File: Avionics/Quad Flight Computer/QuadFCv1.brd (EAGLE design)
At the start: 49.5 x 49.5 mm, 122 parts, among them J2 1050270001, Q1 DMP2035U, Q2 DMP2035U, Q3 DMP2035U, SW1 PTS635VL31-VERT, U1 TM4C123GH6PZ, U10 LTC4412, U11 AP7215-33YG-13, U2 74LVC4245APW, U3 ATMEGA32U2-MU, U5 INVESENSE_MPU-6000, U6 HMC5883LSMD, U7 MS5611-01BA, U8 74AUP1G19GW, U9 S25FL127S, X1 HWB, Y1 32.768KHZ, Y2 AWSCR-20.00CW-T, Y3 PRQC16.00SR5010X000

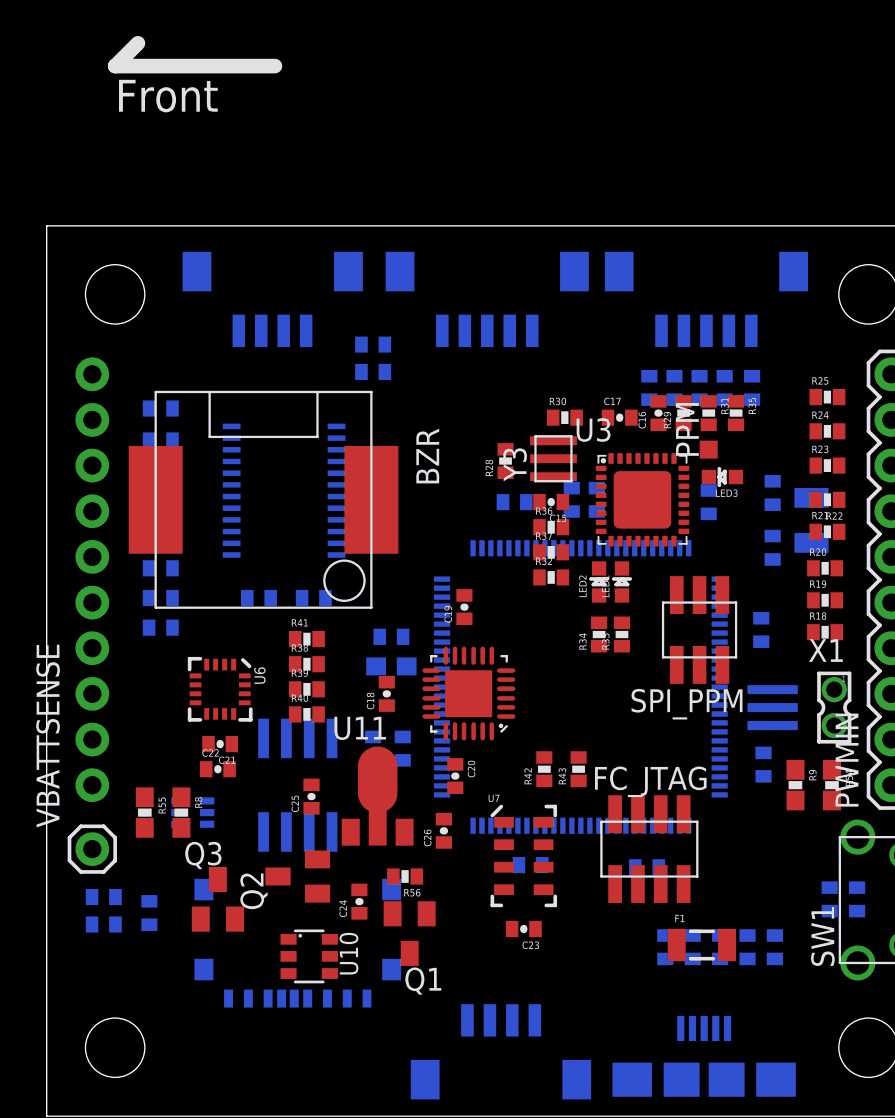
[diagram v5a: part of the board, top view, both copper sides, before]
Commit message: Refactored power distrib board libraries into single library
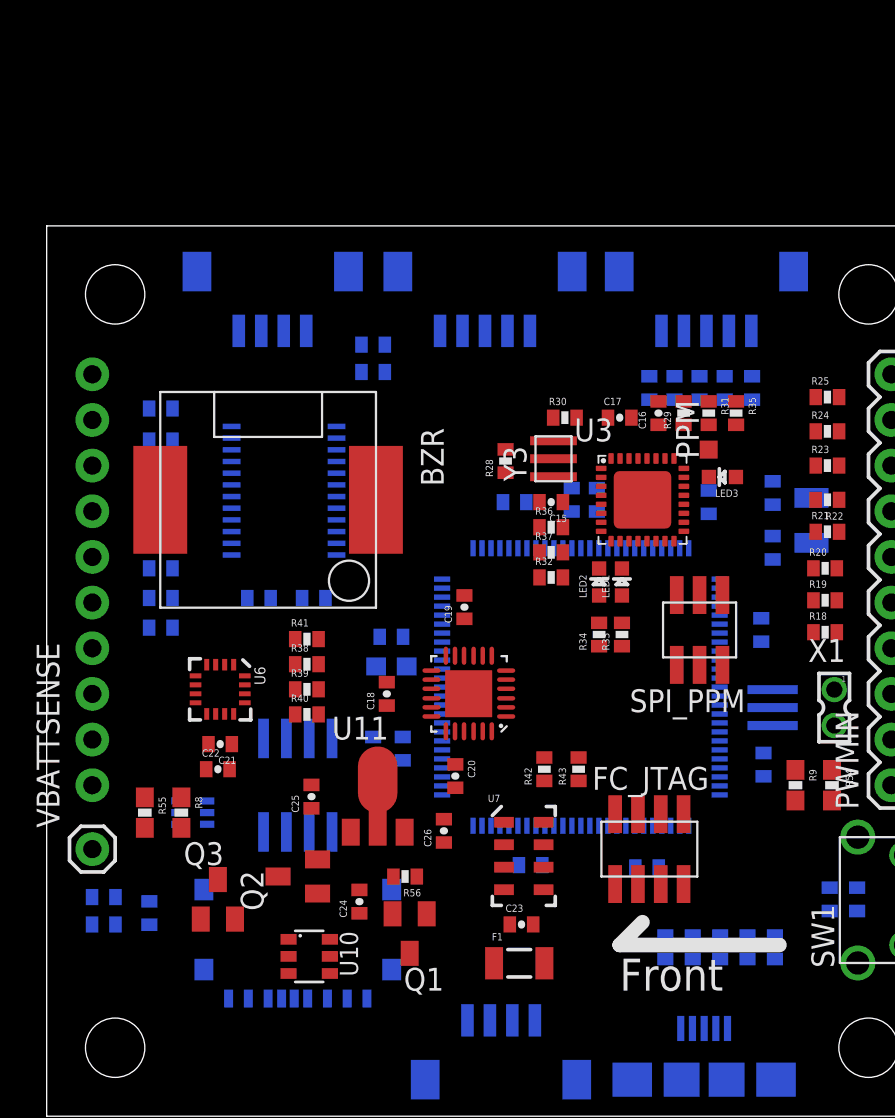
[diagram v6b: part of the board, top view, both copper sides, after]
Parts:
- moved F1 10.2 mm to (26.3, 8.51)
- moved C23 0.28 mm to (26.4, 10.7), turned to 0 degrees
- moved BZR 0.25 mm to (12.3, 34.3)
- moved RADIO1 0.13 mm to (24.4, 43.7)
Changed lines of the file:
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@@
 <setting verticaltext="up"/>
 </settings>
-<grid distance="0.005" unitdist="inch" unit="inch" style="lines" multiple="1" display="no" altdistance="0.025" altunitdist="inch" altunit="inch"/>
+<grid distance="0.005" unitdist="inch" unit="mm" style="lines" multiple="1" display="no" altdistance="0.025" altunitdist="inch" altunit="inch"/>
 <layers>
 <layer number="1" name="Top" color="4" fill="1" visible="yes" active="yes"/>
@@
 <layer number="220" name="220bmp" color="21" fill="1" visible="no" active="no"/>
 <layer number="221" name="221bmp" color="22" fill="1" visible="no" active="no"/>
-<layer number="222" name="222bmp" color="23" fill="1" visible="no" active="no"/>
 <layer number="223" name="223bmp" color="24" fill="1" visible="no" active="no"/>
 <layer number="224" name="224bmp" color="25" fill="1" visible="no" active="no"/>
@@
 <wire x1="49.51" y1="49.53" x2="0" y2="49.53" width="0" layer="20"/>
 <wire x1="0" y1="49.53" x2="0" y2="0" width="0" layer="20"/>
-<wire x1="12.7" y1="58.42" x2="3.81" y2="58.42" width="0.8128" layer="21"/>
-<wire x1="3.81" y1="58.42" x2="5.08" y2="59.69" width="0.8128" layer="21"/>
-<text x="3.81" y="55.88" size="1.778" layer="21">Front</text>
+<wire x1="40.767" y1="9.525" x2="31.877" y2="9.525" width="0.8128" layer="21"/>
+<wire x1="31.877" y1="9.525" x2="33.147" y2="10.795" width="0.8128" layer="21"/>
+<text x="31.877" y="6.985" size="1.778" layer="21">Front</text>
 </plain>
 <attributes>
@@
 <element name="R35" library="QuadFCv1" package="0402-RES" value="1k" x="38.354" y="39.116" rot="R270"/>
 <element name="LED3" library="QuadFCv1" package="SPARKFUN_LED-0603" value="GREEN" x="37.592" y="35.56" rot="R90"/>
-<element name="F1" library="QuadFCv1" package="PTC-1206" value="500mA" x="36.449" y="9.525"/>
+<element name="F1" library="QuadFCv1" package="PTC-1206" value="500mA" x="26.289" y="8.509"/>
 <element name="Y3" library="QuadFCv1" package="PRQC16.00SR5010X000" value="PRQC16.00SR5010X000" x="28.194" y="36.576" rot="R90"/>
 <element name="R36" library="QuadFCv1" package="0402-RES" value="1k" x="28.067" y="32.766"/>
@@
 <attribute name="LINK" value="http://www.meas-spec.com/product/t_product.aspx?id=8503#" x="22.098" y="22.098" size="1.778" layer="27" display="off"/>
 </element>
-<element name="C23" library="QuadFCv1" package="0402-CAP" value="0.1uF" x="26.543" y="10.414" rot="R180"/>
+<element name="C23" library="QuadFCv1" package="0402-CAP" value="0.1uF" x="26.416" y="10.668"/>
 <element name="R41" library="QuadFCv1" package="0402-RES" value="0" x="14.478" y="26.543"/>
 <element name="R40" library="QuadFCv1" package="0402-RES" value="0" x="14.478" y="22.352"/>
@@
 <element name="C25" library="QuadFCv1" package="0402-CAP" value="1u" x="14.732" y="17.78" rot="R90"/>
 <element name="C26" library="QuadFCv1" package="0402-CAP" value="1u" x="22.098" y="15.875" rot="R90"/>
-<element name="RADIO1" library="QuadFCv1" package="DF13_5POS" value="" x="24.511" y="43.688" rot="MR0"/>
+<element name="RADIO1" library="QuadFCv1" package="DF13_5POS" value="" x="24.384" y="43.688" rot="MR0"/>
 <element name="U12" library="QuadFCv1" package="USB-AB-MICRO-SMD" value="" x="36.576" y="2.032" rot="MR90"/>
 <element name="SW1" library="QuadFCv1" package="PTS635VL31" value="PTS635VL31-VERT" x="47.625" y="9.525" rot="R90"/>
-<element name="BZR" library="QuadFCv1" package="CMT-1203-SMT" value="CMT-1203-SMT" x="12.065" y="34.29" rot="R270"/>
+<element name="BZR" library="QuadFCv1" package="CMT-1203-SMT" value="CMT-1203-SMT" x="12.319" y="34.29" rot="R270"/>
 </elements>
 <signals>
@@
 <wire x1="27.218" y1="16.156" x2="25.443" y2="16.353" width="0" layer="19" extent="1-16"/>
 <wire x1="27.574" y1="13.97" x2="27.218" y2="16.156" width="0" layer="19" extent="16-16"/>
-<wire x1="27.193" y1="10.414" x2="27.574" y2="13.97" width="0" layer="19" extent="1-16"/>
+<wire x1="25.766" y1="10.668" x2="27.574" y2="13.97" width="0" layer="19" extent="1-16"/>
 <wire x1="27.686" y1="19.954" x2="27.218" y2="16.156" width="0" layer="19" extent="1-16"/>
 <wire x1="29.591" y1="19.954" x2="27.686" y2="19.954" width="0" layer="19" extent="1-1"/>
@@
 <wire x1="8.902" y1="25.119" x2="9.902" y2="25.119" width="0" layer="19" extent="1-1"/>
 <wire x1="11.022" y1="22.999" x2="9.902" y2="25.119" width="0" layer="19" extent="1-1"/>
-<wire x1="23.408" y1="5.334" x2="27.193" y2="10.414" width="0" layer="19" extent="1-16"/>
+<wire x1="23.408" y1="5.334" x2="25.766" y2="10.668" width="0" layer="19" extent="1-16"/>
 <wire x1="7.328" y1="16.891" x2="11.022" y2="22.999" width="0" layer="19" extent="1-16"/>
 <wire x1="12.065" y1="15.815" x2="7.328" y2="16.891" width="0" layer="19" extent="16-16"/>
 <wire x1="13.07" y1="6.548" x2="12.065" y2="15.815" width="0" layer="19" extent="16-16"/>
 <wire x1="43.561" y1="11.415" x2="39.878" y2="20.208" width="0" layer="19" extent="16-16"/>
-<wire x1="23.261" y1="43.688" x2="26.685" y2="34.163" width="0" layer="19" extent="16-16"/>
-<wire x1="18.811" y1="42.926" x2="23.261" y2="43.688" width="0" layer="19" extent="16-16"/>
+<wire x1="23.134" y1="43.688" x2="26.685" y2="34.163" width="0" layer="19" extent="16-16"/>
+<wire x1="18.811" y1="42.926" x2="23.134" y2="43.688" width="0" layer="19" extent="16-16"/>
 </signal>
 <signal name="GND">
@@
 <wire x1="26.274" y1="13.97" x2="25.443" y2="13.853" width="0" layer="19" extent="1-16"/>
 <wire x1="27.643" y1="12.603" x2="26.274" y2="13.97" width="0" layer="19" extent="1-16"/>
+<wire x1="27.066" y1="10.668" x2="27.643" y2="12.603" width="0" layer="19" extent="1-1"/>
 <wire x1="26.718" y1="16.156" x2="26.274" y2="13.97" width="0" layer="19" extent="16-16"/>
-<wire x1="25.893" y1="10.414" x2="27.643" y2="12.603" width="0" layer="19" extent="1-1"/>
 <wire x1="17.399" y1="11.288" x2="16.916" y2="15.799" width="0" layer="19" extent="1-1"/>
 <wire x1="13.455" y1="8.89" x2="17.399" y2="11.288" width="0" layer="19" extent="1-1"/>
 <wire x1="13.455" y1="7.94" x2="13.455" y2="8.89" width="0" layer="19" extent="1-1"/>
 <wire x1="15.62" y1="6.548" x2="13.455" y2="7.94" width="0" layer="19" extent="1-16"/>
-<wire x1="27.158" y1="5.334" x2="25.893" y2="10.414" width="0" layer="19" extent="1-16"/>
 <wire x1="32.751" y1="13.843" x2="27.643" y2="12.603" width="0" layer="19" extent="1-16"/>
 <wire x1="34.163" y1="12.9159" x2="32.751" y2="13.843" width="0" layer="19" extent="1-16"/>
 <wire x1="35.433" y1="12.9159" x2="34.163" y2="12.9159" width="0" layer="19" extent="1-1"/>
 <wire x1="33.218" y1="16.156" x2="32.751" y2="13.843" width="0" layer="19" extent="16-16"/>
+<wire x1="27.158" y1="5.334" x2="27.066" y2="10.668" width="0" layer="19" extent="1-16"/>
 <wire x1="8.928" y1="16.891" x2="14.732" y2="18.43" width="0" layer="19" extent="1-16"/>
 <wire x1="9.002" y1="20.701" x2="8.928" y2="16.891" width="0" layer="19" extent="1-16"/>
@@
 <wire x1="10.688" y1="43.688" x2="10.2902" y2="38.373" width="0" layer="19" extent="16-16"/>
 <wire x1="16.1258" y1="38.373" x2="10.2902" y2="38.373" width="0" layer="19" extent="16-16"/>
-<wire x1="22.011" y1="43.688" x2="16.1258" y2="38.373" width="0" layer="19" extent="16-16"/>
+<wire x1="21.884" y1="43.688" x2="16.1258" y2="38.373" width="0" layer="19" extent="16-16"/>
 </signal>
 <signal name="5V">
@@
 <wire x1="30.847" y1="34.54" x2="31.397" y2="36.59" width="0" layer="19" extent="1-1"/>
 <wire x1="28.717" y1="34.163" x2="30.847" y2="34.54" width="0" layer="19" extent="1-1"/>
-<wire x1="27.011" y1="43.688" x2="31.227" y2="38.862" width="0" layer="19" extent="1-16"/>
+<wire x1="26.884" y1="43.688" x2="31.227" y2="38.862" width="0" layer="19" extent="1-16"/>
 <wire x1="30.734" y1="26.147" x2="28.717" y2="34.163" width="0" layer="19" extent="1-1"/>
 <wire x1="32.004" y1="26.147" x2="30.734" y2="26.147" width="0" layer="19" extent="1-1"/>
 <wire x1="37.592" y1="28.9941" x2="32.004" y2="26.147" width="0" layer="19" extent="1-1"/>
-<wire x1="18.811" y1="41.402" x2="27.011" y2="43.688" width="0" layer="19" extent="16-16"/>
+<wire x1="18.811" y1="41.402" x2="26.884" y2="43.688" width="0" layer="19" extent="16-16"/>
 <wire x1="43.688" y1="17.565" x2="37.592" y2="28.9941" width="0" layer="19" extent="1-1"/>
 <wire x1="10.2902" y1="31.223" x2="18.811" y2="41.402" width="0" layer="19" extent="16-16"/>
@@
 <contactref element="Q1" pad="3"/>
 <contactref element="Q3" pad="2"/>
-<wire x1="20.193" y1="9.06" x2="35.049" y2="9.525" width="0" layer="19" extent="1-1"/>
+<wire x1="20.193" y1="9.06" x2="24.889" y2="8.509" width="0" layer="19" extent="1-1"/>
 <wire x1="10.475" y1="10.965" x2="20.193" y2="9.06" width="0" layer="19" extent="1-1"/>
 </signal>
@@
 <contactref element="U12" pad="VBUS"/>
 <contactref element="F1" pad="2"/>
-<wire x1="37.876" y1="4.882" x2="37.849" y2="9.525" width="0" layer="19" extent="1-16"/>
+<wire x1="27.689" y1="8.509" x2="37.876" y2="4.882" width="0" layer="19" extent="1-16"/>
 </signal>
 </signals>

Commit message: Minor updates.
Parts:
- moved GPS 2.65 mm to (12.4, 43.7)
- moved I2C 2.59 mm to (25.1, 5.33)
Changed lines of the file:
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@@
 <layer number="220" name="220bmp" color="21" fill="1" visible="no" active="no"/>
 <layer number="221" name="221bmp" color="22" fill="1" visible="no" active="no"/>
+<layer number="222" name="222bmp" color="7" fill="1" visible="yes" active="yes"/>
 <layer number="223" name="223bmp" color="24" fill="1" visible="no" active="no"/>
 <layer number="224" name="224bmp" color="25" fill="1" visible="no" active="no"/>
@@
 <element name="R50" library="QuadFCv1" package="0402-RES" value="10k" x="37.719" y="40.513" rot="MR270"/>
 <element name="R51" library="QuadFCv1" package="0402-RES" value="10k" x="39.243" y="40.513" rot="MR270"/>
-<element name="I2C" library="QuadFCv1" package="DF13_4POS" value="" x="24.638" y="2.794" rot="MR180"/>
-<element name="GPS" library="QuadFCv1" package="DF13_4POS" value="" x="13.208" y="46.228" rot="MR0"/>
+<element name="I2C" library="QuadFCv1" package="DF13_4POS" value="" x="25.146" y="5.334" rot="MR180"/>
+<element name="GPS" library="QuadFCv1" package="DF13_4POS" value="" x="12.446" y="43.688" rot="MR0"/>
 <element name="R52" library="QuadFCv1" package="0402-RES" value="0" x="18.161" y="41.402" rot="MR180"/>
 <element name="R53" library="QuadFCv1" package="0402-RES" value="DNP" x="18.161" y="42.926" rot="MR180"/>
@@
 <wire x1="8.902" y1="25.119" x2="9.902" y2="25.119" width="0" layer="19" extent="1-1"/>
 <wire x1="11.022" y1="22.999" x2="9.902" y2="25.119" width="0" layer="19" extent="1-1"/>
-<wire x1="23.408" y1="5.334" x2="25.766" y2="10.668" width="0" layer="19" extent="1-16"/>
+<wire x1="23.281" y1="5.334" x2="25.766" y2="10.668" width="0" layer="19" extent="1-16"/>
 <wire x1="7.328" y1="16.891" x2="11.022" y2="22.999" width="0" layer="19" extent="1-16"/>
 <wire x1="12.065" y1="15.815" x2="7.328" y2="16.891" width="0" layer="19" extent="16-16"/>
@@
 <wire x1="35.433" y1="12.9159" x2="34.163" y2="12.9159" width="0" layer="19" extent="1-1"/>
 <wire x1="33.218" y1="16.156" x2="32.751" y2="13.843" width="0" layer="19" extent="16-16"/>
-<wire x1="27.158" y1="5.334" x2="27.066" y2="10.668" width="0" layer="19" extent="1-16"/>
+<wire x1="27.031" y1="5.334" x2="27.066" y2="10.668" width="0" layer="19" extent="1-16"/>
 <wire x1="8.928" y1="16.891" x2="14.732" y2="18.43" width="0" layer="19" extent="1-16"/>
 <wire x1="9.002" y1="20.701" x2="8.928" y2="16.891" width="0" layer="19" extent="1-16"/>
@@
 <wire x1="10.2902" y1="37.723" x2="12.461" y2="28.829" width="0" layer="19" extent="16-16"/>
 <wire x1="10.2902" y1="38.373" x2="10.2902" y2="37.723" width="0" layer="19" extent="16-16"/>
-<wire x1="10.688" y1="43.688" x2="10.2902" y2="38.373" width="0" layer="19" extent="16-16"/>
+<wire x1="10.561" y1="43.688" x2="10.2902" y2="38.373" width="0" layer="19" extent="16-16"/>
 <wire x1="16.1258" y1="38.373" x2="10.2902" y2="38.373" width="0" layer="19" extent="16-16"/>
 <wire x1="21.884" y1="43.688" x2="16.1258" y2="38.373" width="0" layer="19" extent="16-16"/>
@@
 <contactref element="R53" pad="1"/>
 <wire x1="17.511" y1="42.926" x2="17.511" y2="41.402" width="0" layer="19" extent="16-16"/>
-<wire x1="14.438" y1="43.688" x2="17.511" y2="42.926" width="0" layer="19" extent="16-16"/>
+<wire x1="14.311" y1="43.688" x2="17.511" y2="42.926" width="0" layer="19" extent="16-16"/>
 </signal>
 <signal name="GPS_TX">
